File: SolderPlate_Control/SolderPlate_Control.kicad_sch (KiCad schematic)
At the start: 23 parts, among them J1 Encoder, J2 Conn_01x04, Q1 Si2301CDS, Q3 BSS138, Q4 Si2301CDS, U1 PEL12D

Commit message: Reduced Encoder control circuit to fit
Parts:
- removed C3: 100nF, Capacitor_SMD:C_0603_1608Metric, symbol Device:C_Small
- removed J2: Conn_01x04, Connector_PinHeader_2.54mm:PinHeader_1x04_P2.54mm_Vertical, symbol Connector_Generic:Conn_01x04
- removed Q3: BSS138, Package_TO_SOT_SMD:SOT-23, symbol Transistor_FET:BSS138
- removed R11: 470, Resistor_SMD:R_0603_1608Metric, symbol Device:R_Small
- removed R12: 68, Resistor_SMD:R_0603_1608Metric, symbol Device:R_Small
- removed R8: 10K, Resistor_SMD:R_0603_1608Metric, symbol Device:R_Small
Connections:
- net Contrast: no longer names the net of J1.6 (Pin_6)
- no-connect marks 0 -> 1

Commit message: Added schematic PDFs
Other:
- title: (none) -> Solder Plate - Control Board
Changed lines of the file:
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@@
 (kicad_sch (version 20230121) (generator eeschema)
   (paper "A4")
+  (title_block
+    (title "Solder Plate - Control Board")
+    (rev "A")
+    (comment 1 "TiZed")
+  )
   (junction (at 167.64 77.47) (diameter 0) (color 0 0 0 0)
   )

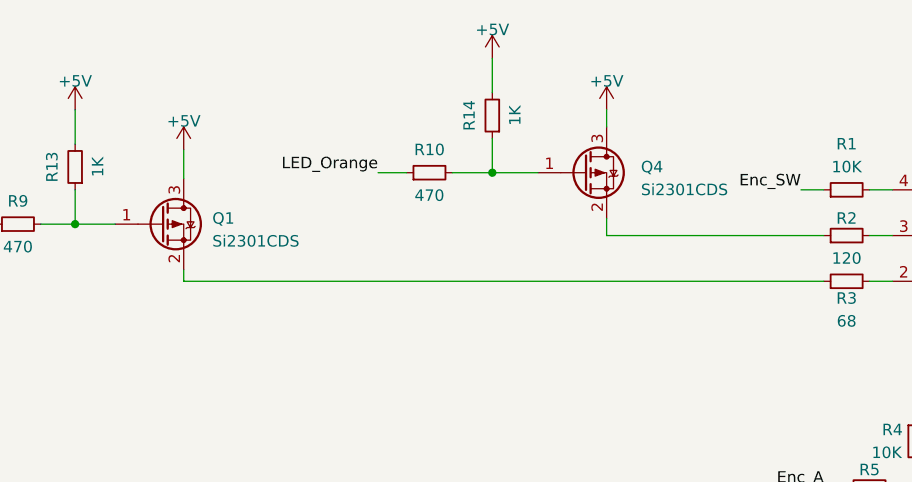
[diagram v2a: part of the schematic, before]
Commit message: Fixed wrongly routed P-MOSs in encoder control PCB
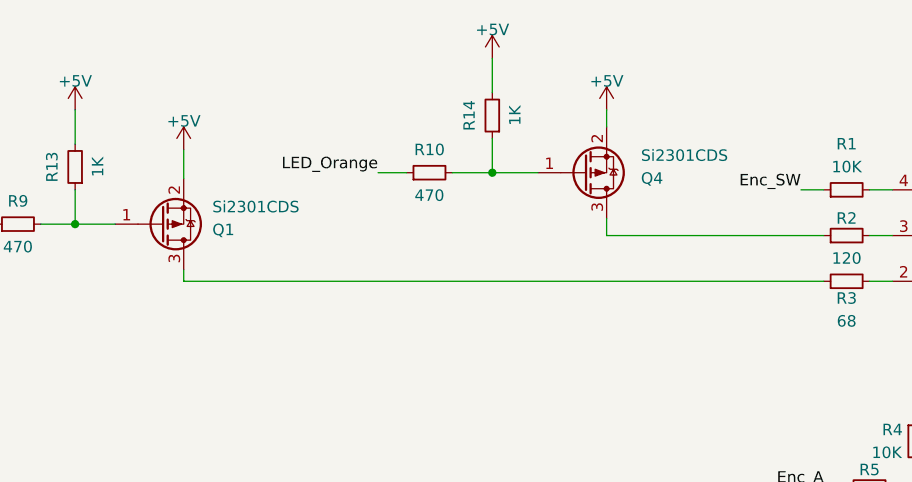
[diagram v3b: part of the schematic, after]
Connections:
- net +5V: now also Q1.2 (S), Q4.2 (S); no longer Q1.3 (D), Q4.3 (D)
- net at R2.1: now also Q4.3 (D); no longer Q4.2 (S)
- net at R3.1: now also Q1.3 (D); no longer Q1.2 (S)
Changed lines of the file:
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@@
     )
   )
-  (symbol (lib_id "Transistor_FET:TSM2301ACX") (at 130.81 42.545 0) (unit 1)
-    (in_bom yes) (on_board yes) (dnp no) (fields_autoplaced)
-    (property "Reference" "Q4" (at 137.16 41.91 0)
+  (symbol (lib_id "Transistor_FET:TSM2301ACX") (at 130.81 42.545 0) (mirror x) (unit 1)
+    (in_bom yes) (on_board yes) (dnp no)
+    (property "Reference" "Q4" (at 137.16 43.18 0)
       (effects (font (size 1.27 1.27)) (justify left))
     )
-    (property "Value" "Si2301CDS" (at 137.16 44.45 0)
+    (property "Value" "Si2301CDS" (at 137.16 40.64 0)
       (effects (font (size 1.27 1.27)) (justify left))
     )
-    (property "Footprint" "Package_TO_SOT_SMD:SOT-23" (at 135.89 44.45 0)
+    (property "Footprint" "Package_TO_SOT_SMD:SOT-23" (at 135.89 40.64 0)
       (effects (font (size 1.27 1.27) italic) (justify left) hide)
     )
@@
     )
   )
-  (symbol (lib_id "Transistor_FET:TSM2301ACX") (at 83.82 48.26 0) (unit 1)
-    (in_bom yes) (on_board yes) (dnp no) (fields_autoplaced)
-    (property "Reference" "Q1" (at 89.535 47.625 0)
+  (symbol (lib_id "Transistor_FET:TSM2301ACX") (at 83.82 48.26 0) (mirror x) (unit 1)
+    (in_bom yes) (on_board yes) (dnp no)
+    (property "Reference" "Q1" (at 89.535 48.895 0)
       (effects (font (size 1.27 1.27)) (justify left))
     )
-    (property "Value" "Si2301CDS" (at 89.535 50.165 0)
+    (property "Value" "Si2301CDS" (at 89.535 46.355 0)
       (effects (font (size 1.27 1.27)) (justify left))
     )
-    (property "Footprint" "Package_TO_SOT_SMD:SOT-23" (at 88.9 50.165 0)
+    (property "Footprint" "Package_TO_SOT_SMD:SOT-23" (at 88.9 46.355 0)
       (effects (font (size 1.27 1.27) italic) (justify left) hide)
     )
